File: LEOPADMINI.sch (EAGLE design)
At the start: 47 parts, among them IC1 ATMEGA32U4-QFN

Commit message: Improved designator positions
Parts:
- C1, C2: value 100nF 0603 -> 100nF
- C3, C4: value 1uF 0603 -> 1uF
- C5, C6: value 15pF 0603 -> 15pF
- R2: value 10K 0603 -> 10K
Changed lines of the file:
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@@
 <?xml version="1.0" encoding="utf-8"?>
 <!DOCTYPE eagle SYSTEM "eagle.dtd">
-<eagle version="9.2.2">
+<eagle version="9.4.0">
 <drawing>
 <settings>
@@
 <parts>
 <part name="GND4" library="SparkFun" deviceset="GND" device=""/>
-<part name="C2" library="freetronics-master-v1.1" deviceset="CAP" device="0603" value="100nF 0603"/>
+<part name="C2" library="freetronics-master-v1.1" deviceset="CAP" device="0603" value="100nF"/>
 <part name="GND3" library="SparkFun" deviceset="GND" device=""/>
 <part name="U$3" library="SparkFun" deviceset="5V" device=""/>
-<part name="R2" library="freetronics-master-v1.1" deviceset="RESISTOR" device="0603" value="10K 0603"/>
+<part name="R2" library="freetronics-master-v1.1" deviceset="RESISTOR" device="0603" value="10K"/>
 <part name="U$1" library="SparkFun" deviceset="5V" device=""/>
-<part name="C3" library="freetronics-master-v1.1" deviceset="CAP" device="0603" value="1uF 0603"/>
-<part name="C1" library="freetronics-master-v1.1" deviceset="CAP" device="0603" value="100nF 0603"/>
+<part name="C3" library="freetronics-master-v1.1" deviceset="CAP" device="0603" value="1uF"/>
+<part name="C1" library="freetronics-master-v1.1" deviceset="CAP" device="0603" value="100nF"/>
 <part name="GND11" library="SparkFun" deviceset="GND" device=""/>
 <part name="ICSP" library="pinhead" deviceset="PINHD-2X3" device="" value="ICSP"/>
@@
 <part name="IC1" library="freetronics-jon" deviceset="ATMEGA32U4" device="-QFN"/>
 <part name="GND15" library="SparkFun" deviceset="GND" device=""/>
-<part name="C5" library="freetronics-master-v1.1" deviceset="CAP" device="0603" value="15pF 0603"/>
-<part name="C6" library="freetronics-master-v1.1" deviceset="CAP" device="0603" value="15pF 0603"/>
+<part name="C5" library="freetronics-master-v1.1" deviceset="CAP" device="0603" value="15pF"/>
+<part name="C6" library="freetronics-master-v1.1" deviceset="CAP" device="0603" value="15pF"/>
 <part name="GND16" library="SparkFun" deviceset="GND" device=""/>
-<part name="C4" library="freetronics-master-v1.1" deviceset="CAP" device="0603" value="1uF 0603"/>
+<part name="C4" library="freetronics-master-v1.1" deviceset="CAP" device="0603" value="1uF"/>
 <part name="GND5" library="SparkFun" deviceset="GND" device=""/>
 <part name="XTL1" library="freetronics-jon" deviceset="CRYSTAL-GND" device="3X2" value="16MHz"/>

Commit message: Replaced most parts using SuperHouse library to add 3D models
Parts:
- ICSP: device pinhead:PINHD-2X3 -> SuperHouse-Connectors:ICSPPTH
- S1: device freetronics-original:TAC_SWITCHPTH -> SuperHouse-Switches:TAC_SWITCH6; SPICEPREFIX (none) -> S
- S10, S11, S12, S13, S14, S15, S16, S17, S18, S19, S2, S20, S3, S4, S5, S6, S7, S8, S9: device freetronics-original:TAC_SWITCHPTH -> SuperHouse-Switches:TAC_SWITCH6

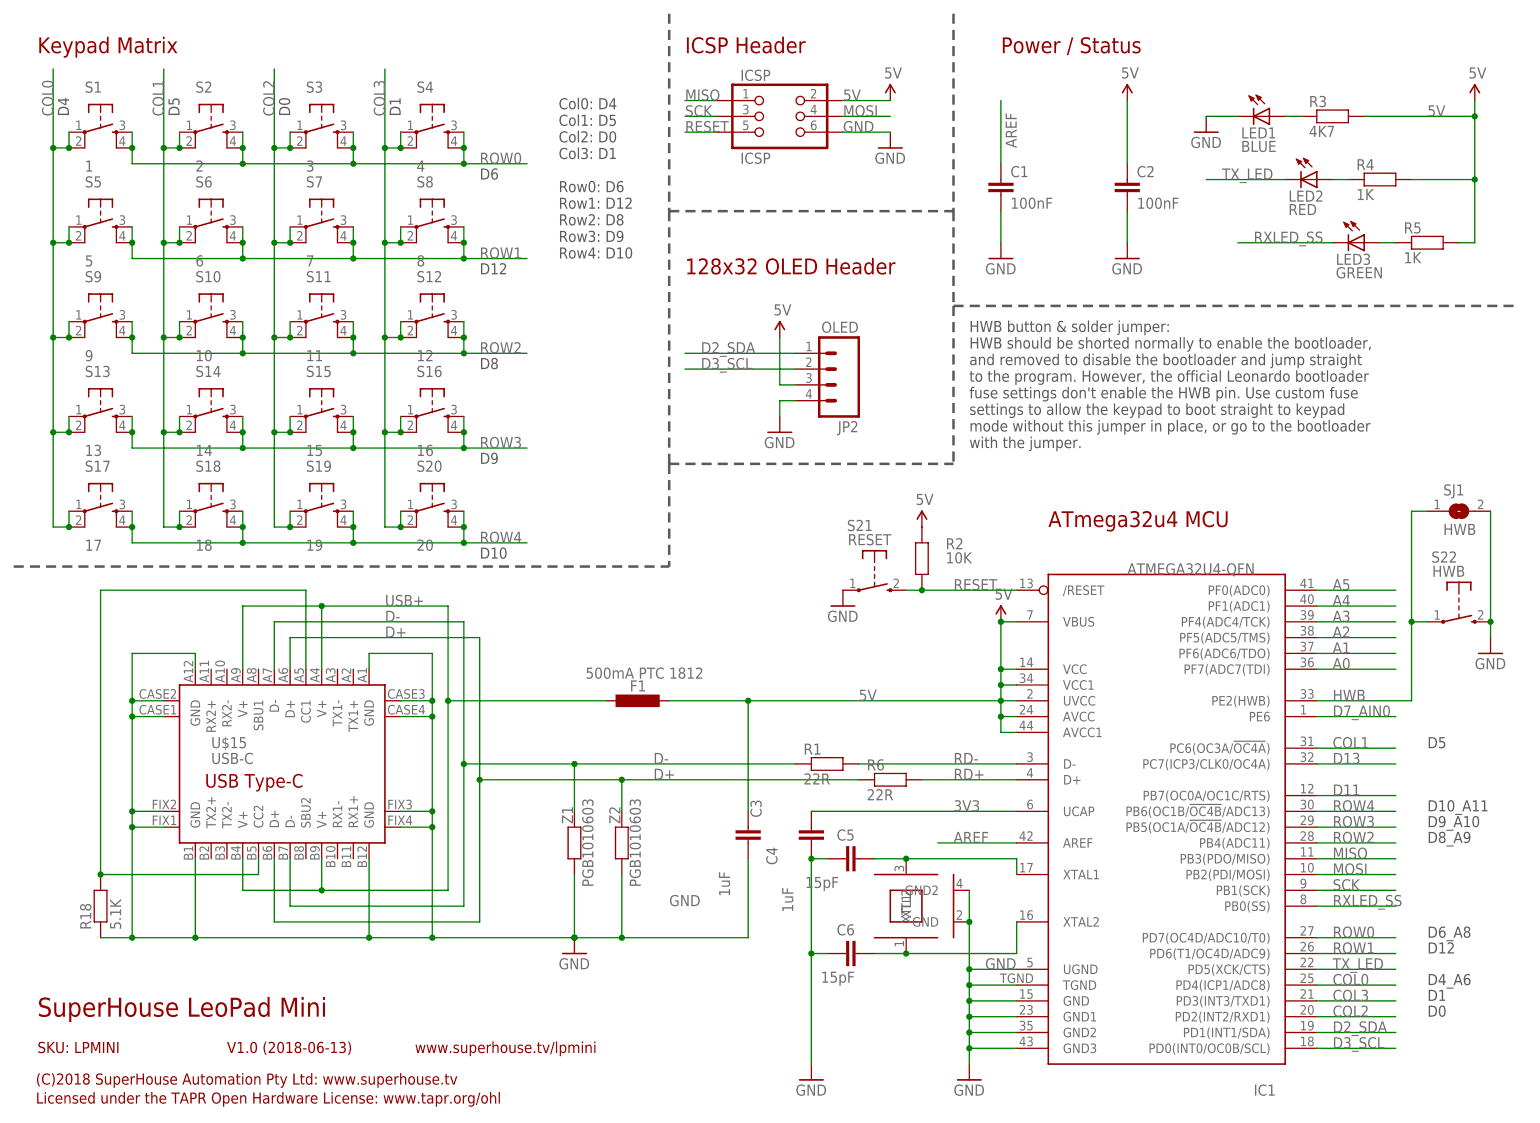
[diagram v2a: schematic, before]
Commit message: Replaced parts using SuperHouse library to add 3D models
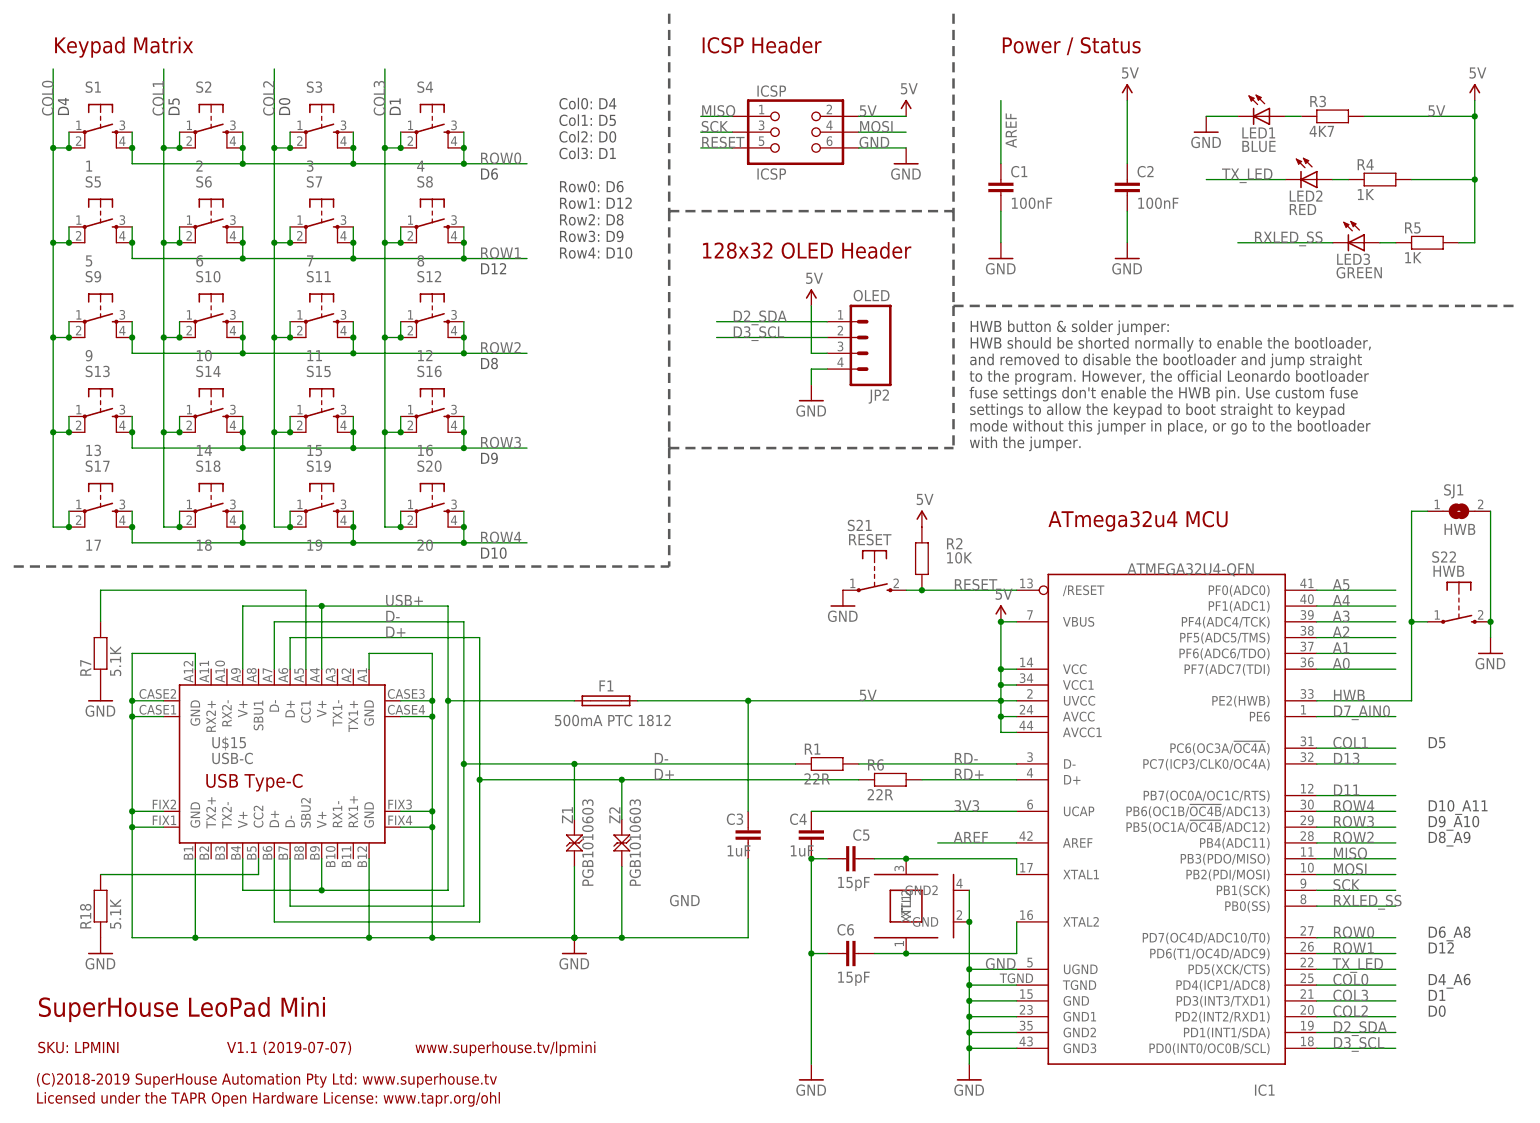
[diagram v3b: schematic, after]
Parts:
- added R7: 5.1K, SuperHouse-DiscreteSemi:RESISTOR0603
- C1, C2, C3, C4, C5, C6: device freetronics-master-v1.1:CAP0603 -> SuperHouse-DiscreteSemi:CAP0603
- F1: device rcl:L-EUL1812 -> SuperHouse-Fuses:PTC050
- LED1, LED2, LED3: device freetronics-jon:LED0603 -> SuperHouse-LEDs:LED0603
- R1, R3, R4, R5, R6: device freetronics-jon:RESISTOR0603 -> SuperHouse-DiscreteSemi:RESISTOR0603
- R18: device freetronics-original:RESISTOR0603 -> SuperHouse-DiscreteSemi:RESISTOR0603
- R2: device freetronics-master-v1.1:RESISTOR0603 -> SuperHouse-DiscreteSemi:RESISTOR0603
- S1, S10, S11, S12, S13, S14, S15, S16, S17, S18, S19, S2, S20, S3, S4, S5, S6, S7, S8, S9: device SuperHouse-Switches:TAC_SWITCH6 -> SuperHouse-Switches:TAC_SWITCH-PTH-6
- S21, S22: device freetronics-jon:TAC_SWITCH_2PINSMT -> SuperHouse-Switches:TAC_SWITCH_2PINSMT
- U$15: device freetronics-jon:USB-C -> SuperHouse-Connectors:USB-C
- XTL1: device freetronics-jon:CRYSTAL-GND3X2 -> SuperHouse-Oscillators:CRYSTAL-GND3X2
- Z1, Z2: device freetronics-master-v1.1:RESISTOR0603 -> SuperHouse-DiscreteSemi:TVS0603
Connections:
- new net N$1: R18.2, U$15.CC2
- net GND: now also R7.1
- net N$67: now also R7.2; no longer R18.2, U$15.CC2
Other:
- note added: "(C)2018-2019 SuperHouse Automation Pty Ltd: www.superhouse.tv"
- note added: "V1.1 (2019-07-07)"
- note removed: "(C)2018 SuperHouse Automation Pty Ltd: www.superhouse.tv"
- note removed: "V1.0 (2018-06-13)"
- moved on the sheet: ICSP, JP2
